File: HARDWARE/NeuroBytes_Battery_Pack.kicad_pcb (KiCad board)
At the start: 2 copper layers, 61 x 56.7 mm, 16 parts, among them P1 JST_GH_5-pos, SW1 Switch_DPDT, U1 LDL212_LDO

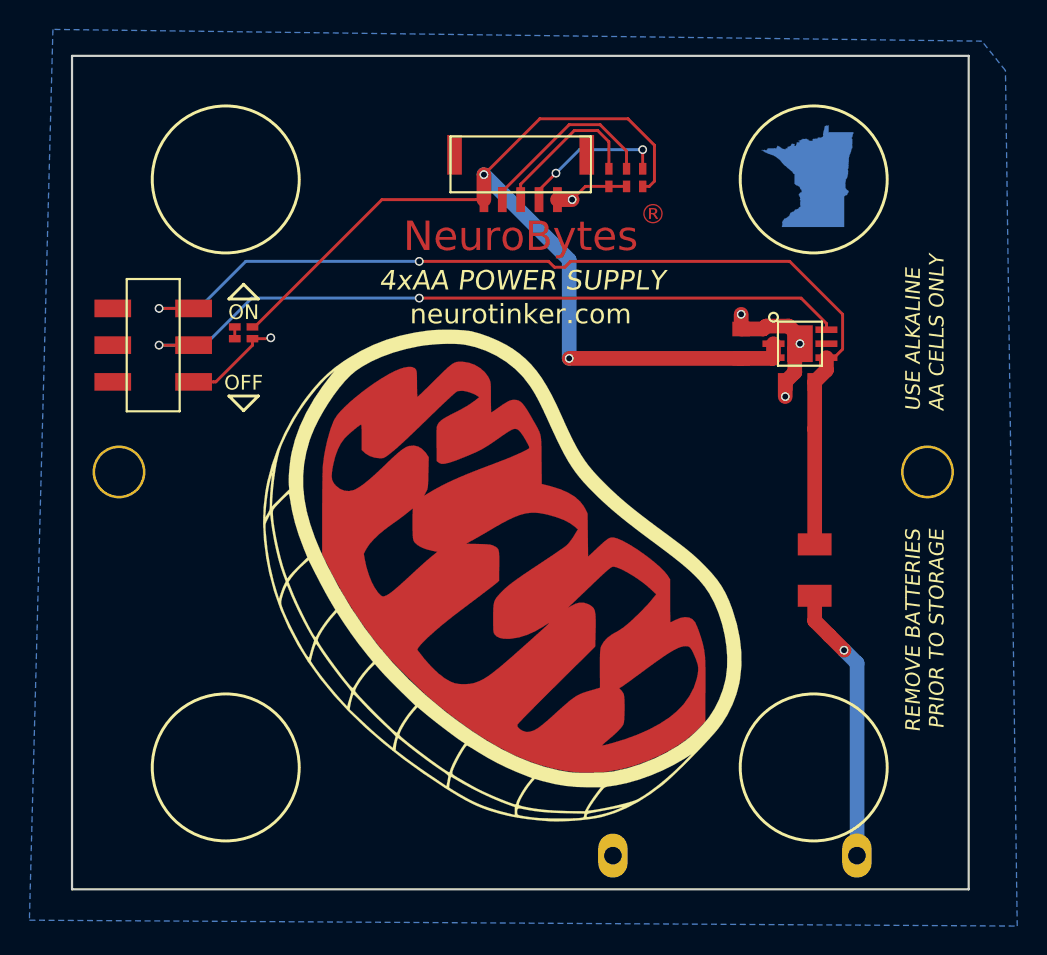
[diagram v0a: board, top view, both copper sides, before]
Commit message: updated to include two 5-pin JST connectors and side-mtg switch. Moved LED to center.
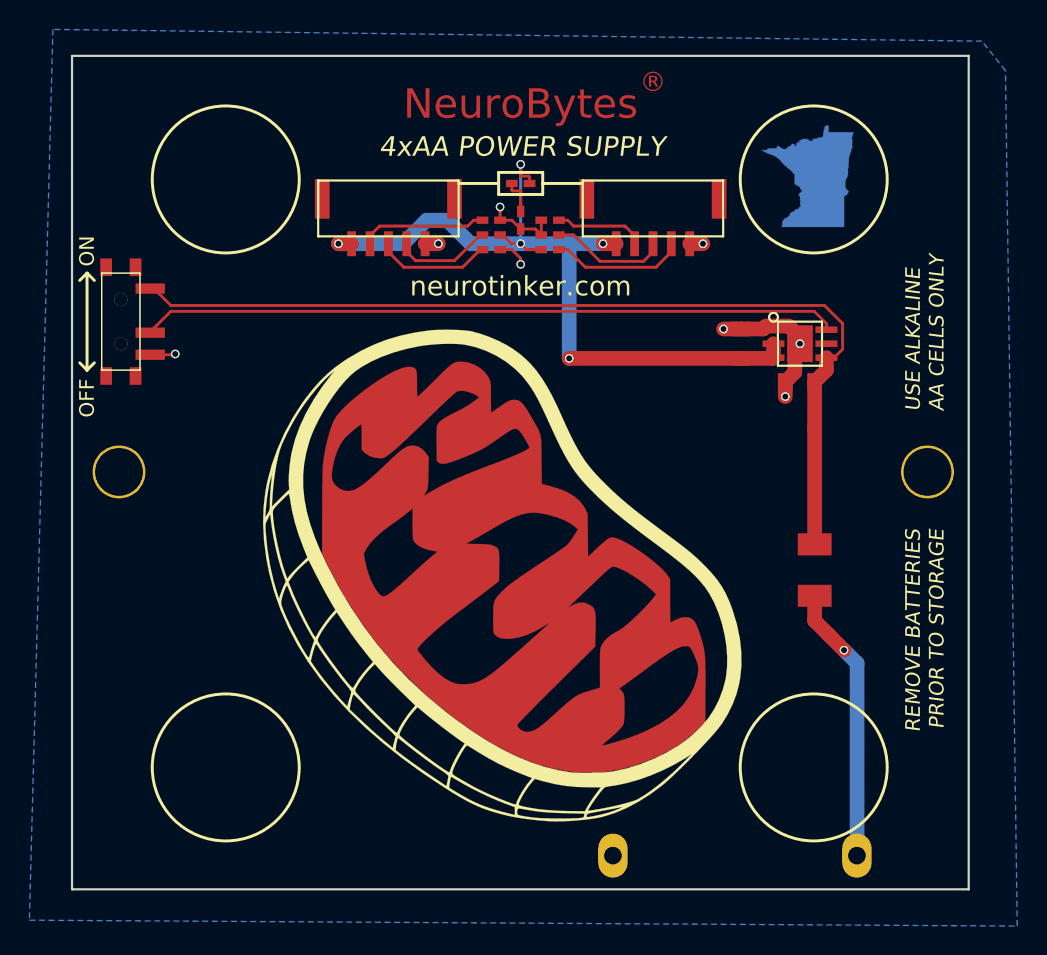
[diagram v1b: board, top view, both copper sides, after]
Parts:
- added P2: JST_GH_5-pos, KiCad_Footprints:ZF_CONN_JST_GH_5POS, F.Cu at (184.0, 47.0)
- added R1: R_Small, KiCad_Footprints:ZF_SMD_NonPol_0402, F.Cu at (177.0, 47.0)
- added R3: R_Small, KiCad_Footprints:ZF_SMD_NonPol_0402, F.Cu at (177.0, 48.0)
- added R7: R_Small, KiCad_Footprints:ZF_SMD_NonPol_0402, F.Cu at (177.0, 49.0)
- SW1: value Switch_DPDT -> Switch_SPDT; footprint KiCad_Footprints:ZF_SW_Slide_DPDT_SMD -> KiCad_Footprints:ZF_SW_PCM12SMTR
- moved D1 21.2 mm to (175.0, 44.5)
- moved R2 20.5 mm to (175.0, 47.0), turned to 270 degrees
- moved R6 11.0 mm to (173.0, 48.0), turned to 0 degrees
- moved R4 9.65 mm to (173.0, 47.0), turned to 0 degrees
- moved P1 9.49 mm to (166.0, 47.0)
- moved R5 9.38 mm to (173.0, 49.0), turned to 0 degrees
- moved SW1 2.72 mm to (147.8, 53.9), turned to 270 degrees
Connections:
- SW1 pad 1: Net-(SW1-Pad1) -> Net-(C1-Pad1)
- SW1 pad 3: Net-(SW1-Pad3) -> GND
- U1 pad 6: Net-(SW1-Pad5) -> Net-(SW1-Pad2)
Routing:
- net Net-(SW1-Pad5): track 50.6 -> 0.00 mm, vias 2 -> 0
- net Net-(SW1-Pad2): track 0.00 -> 47.6 mm
- net Net-(C2-Pad1): track 68.2 -> 54.5 mm, vias 2 -> 5
- net Net-(P2-Pad2): track 0.00 -> 9.13 mm
- net Net-(P2-Pad3): track 0.00 -> 7.96 mm
- net Net-(P2-Pad4): track 0.00 -> 6.13 mm
- net Net-(P1-Pad4): track 12.8 -> 8.63 mm
- net Net-(C1-Pad1): track 68.3 -> 64.4 mm, vias 2 -> 0
- net Net-(P1-Pad2): track 10.1 -> 6.67 mm, vias 2 -> 0
- net Net-(P1-Pad3): track 10.7 -> 8.32 mm
- net Net-(D1-Pad1): track 0.80 -> 2.47 mm
- net GND: track 21.8 -> 20.7 mm, vias 5 -> 8

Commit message: updated component labels and regenerated netlist. generated BOM. minor page layout updates.
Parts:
- C1, C2: value C -> 1u
- R1, R3, R4, R5, R6, R7: value R_Small -> 10k
- R2: value R -> 4k7
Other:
- board text added: "COMPONENT POSITION ORIGIN"
- board text added: "INSTALL FOUR POLYURETHANE BUMBERS IN FOUR 10MM SILKSCREEN CIRCLES"
- board text added: "INSTALL TWO NYLON RIVETS PRIOR TO SOLDERING BATTERY PACK"
- board text added: "NOTES: 1. FOOTPRINTS ORIENTED PER IPC-7351FC LEVEL B (PIN 1 IN LOWER LEFT) 2. COMPONENT ORIENTATION IN DEGREES COUNTER-CLOCKWISE 3. COMPONENTS ARE MOUNTED ON F.CU LAYER ONLY 4. PCB IS 1.6mm FR4 RATED FOR ROHS REFLOW, 1OZ COPPER, ENIG FINISH 5. MATTE BLACK SOLDER MASK WITH WHITE SILKSCREEN 6. SOLDER PASTE MUST BE ROHS COMPLIANT (LEAD-FREE) 7. NO MARKS (E-TEST, QA, SERIAL NUMBER, ETC) ON FRONT (LOG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"
- board text added: "ROUTE TWO SIDES OF PCB"
- board text added: "V-SCORE TWO SIDES OF PCB"
